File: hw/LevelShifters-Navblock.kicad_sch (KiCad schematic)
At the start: 6 parts, among them U4100 SN74LVCH16T245, U4101 SN74LVCH16T245

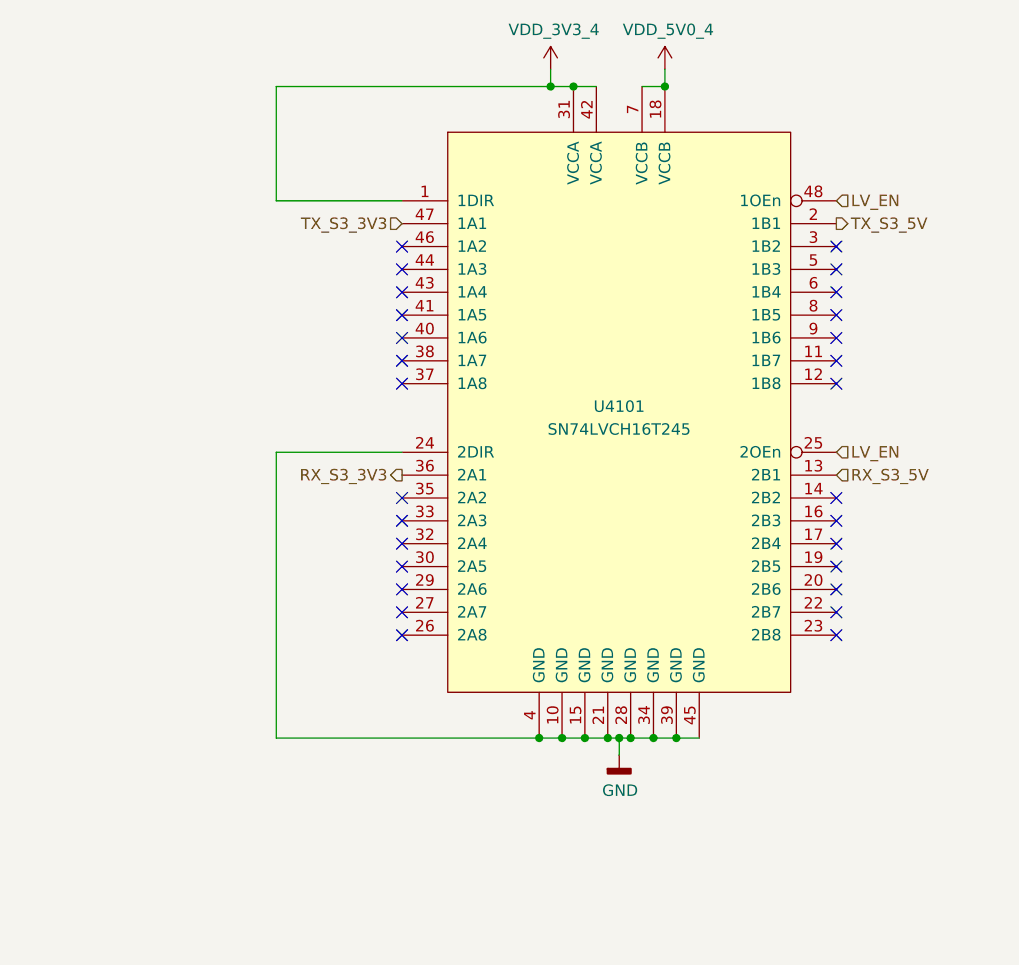
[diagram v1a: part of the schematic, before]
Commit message: Update schematic:
- Add ESD protection.
- Adjust distance bolts so they fit to the MX mounting plate.
- Make key layout symmetric.
- Add resistor to TX driver outputs.
- Use alternate IO functions on inter-board connectors.
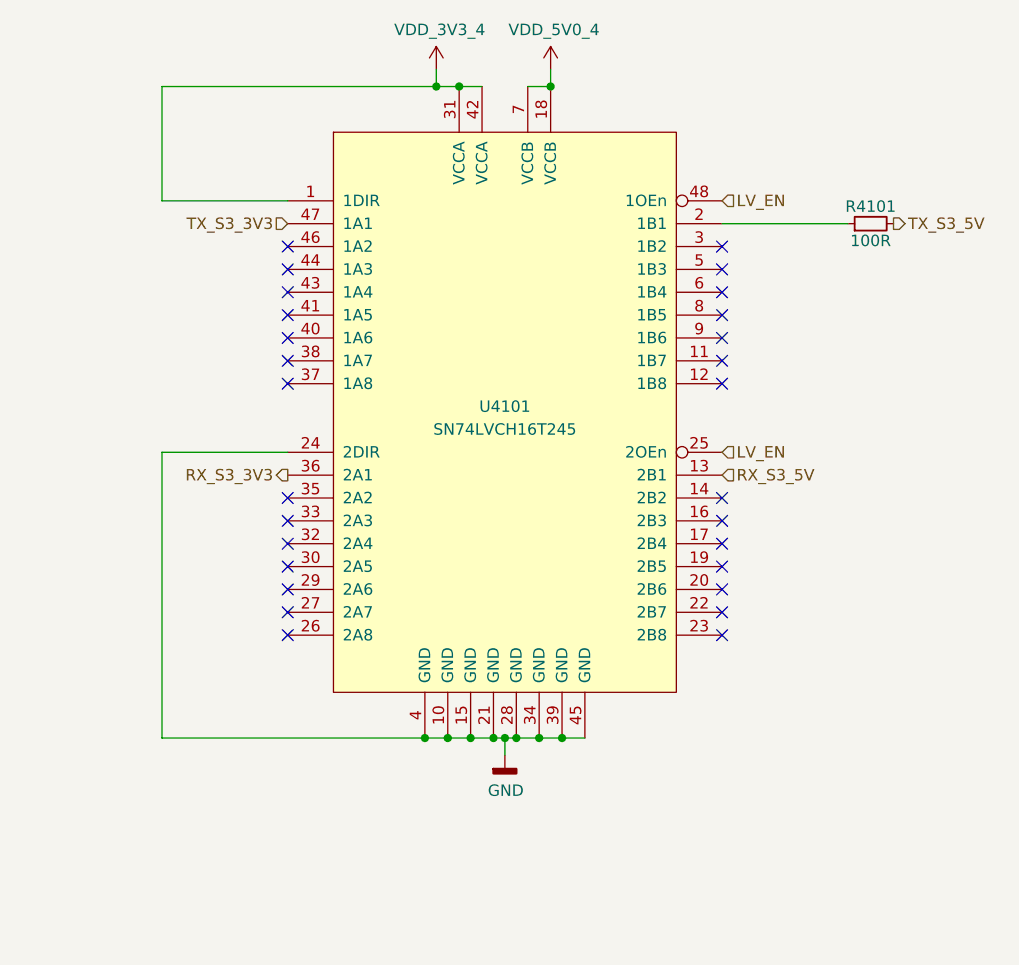
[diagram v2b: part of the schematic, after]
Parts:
- added R4101: 100R, Keyboard:R_0402, symbol Keyboard:100R
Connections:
- net TX_S3_5V: now also R4101.2; no longer U4101.2 (1B1)
- new net: R4101.1, U4101.2 (1B1)
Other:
- moved on the sheet: U4101

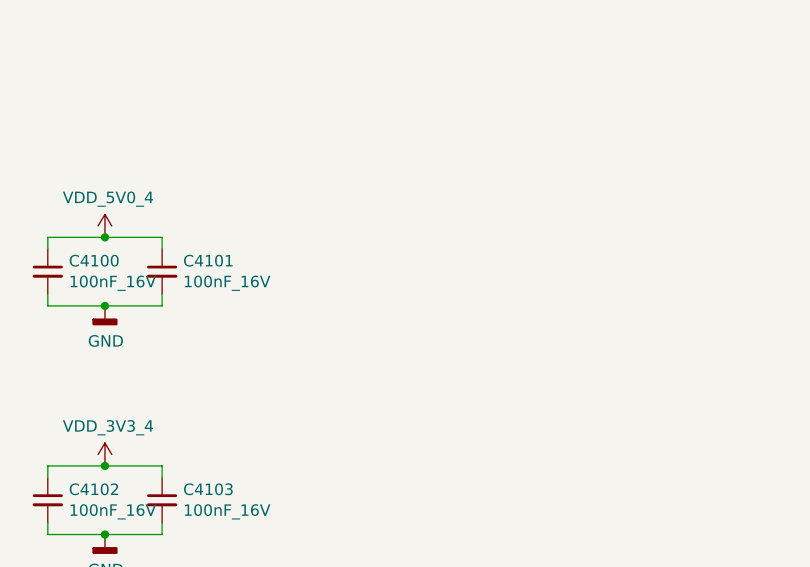
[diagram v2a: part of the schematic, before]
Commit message: Add current probes to 3.3V and pull-up to LV_EN.
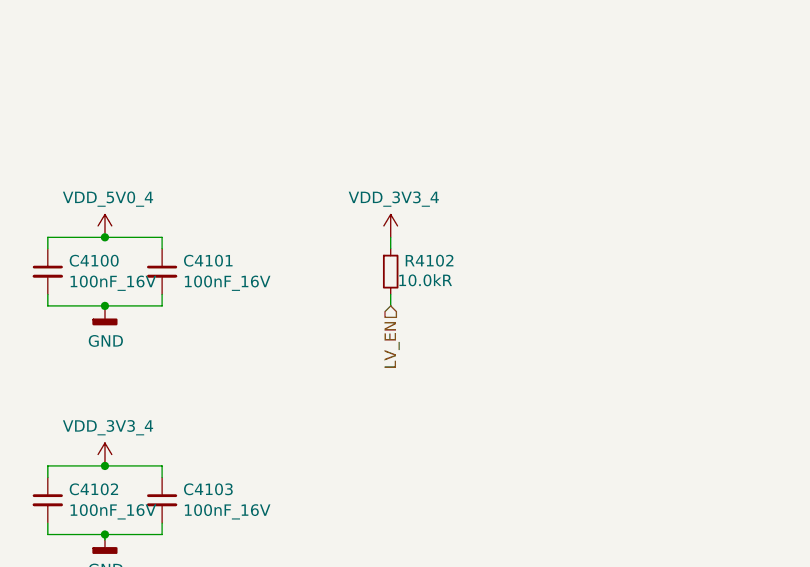
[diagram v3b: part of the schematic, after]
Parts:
- added R4102: 10.0kR, Keyboard:R_0402, symbol Keyboard:10.0kR
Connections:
- net LV_EN: now also R4102.2
- net VDD_3V3_4: now also R4102.1
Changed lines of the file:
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@@
+    (stroke (width 0) (type default) (color 0 0 0 0))
+  )
+  (wire (pts (xy 76.2 146.05) (xy 76.2 147.32))
     (stroke (width 0) (type default) (color 0 0 0 0))
   )
@@
   )
   (wire (pts (xy 38.1 146.05) (xy 38.1 147.32))
+    (stroke (width 0) (type default) (color 0 0 0 0))
+  )
+  (wire (pts (xy 76.2 140.97) (xy 76.2 139.7))
     (stroke (width 0) (type default) (color 0 0 0 0))
   )
@@
   )
   (hierarchical_label "LR9_3V3" (shape input) (at 33.02 87.63 180)
+    (effects (font (size 1.27 1.27)) (justify right))
+  )
+  (hierarchical_label "LV_EN" (shape input) (at 76.2 147.32 270)
     (effects (font (size 1.27 1.27)) (justify right))
   )
@@
     (pin "2")
   )
+  (symbol (lib_id "Keyboard:10.0kR") (at 76.2 143.51 0) (unit 1)
+    (in_bom yes) (on_board yes)
+    (property "Reference" "R4102" (id 0) (at 77.6986 142.3416 0)
+      (effects (font (size 1.27 1.27)) (justify left))
+    )
+    (property "Value" "10.0kR" (id 1) (at 76.962 144.526 0)
+      (effects (font (size 1.27 1.27)) (justify left))
+    )
+    (property "Footprint" "Keyboard:R_0402" (id 2) (at 74.422 145.542 0)
+      (effects (font (size 1.27 1.27)) hide)
+    )
+    (property "Datasheet" "667-ERJ-2RKF1002X" (id 3) (at 76.962 143.002 0)
+      (effects (font (size 1.27 1.27)) hide)
+    )
+    (property "mouser#" "667-ERJ-2RKF1002X" (id 4) (at 79.502 140.462 0)
+      (effects (font (size 1.524 1.524)) hide)
+    )
+    (pin "1")
+    (pin "2")
+  )
+  (symbol (lib_id "Keyboard:VDD_3V3_4") (at 76.2 139.7 0) (unit 1)
+    (in_bom yes) (on_board yes)
+    (property "Reference" "#PWR04113" (id 0) (at 76.2 143.51 0)
+      (effects (font (size 1.27 1.27)) hide)
+    )
+    (property "Value" "VDD_3V3_4" (id 1) (at 76.581 135.3058 0))
+    (property "Footprint" "" (id 2) (at 76.2 139.7 0)
+      (effects (font (size 1.27 1.27)) hide)
+    )
+    (property "Datasheet" "" (id 3) (at 76.2 139.7 0)
+      (effects (font (size 1.27 1.27)) hide)
+    )
+    (pin "1")
+  )
 )
